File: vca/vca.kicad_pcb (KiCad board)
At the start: 4 copper layers, 95 x 100 mm, 132 parts, among them J2 Conn_ARM_JTAG_SWD_10, U1 LM324, U10 LUM-1502-03_3.5mm_mono_vertic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, U11 LUM-1502-03_3.5mm_mono_vertic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, U12 LUM-1502-03_3.5mm_mono_vertic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, U13 LUM-1502-03_3.5mm_mono_vertic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, U14 LUM-1502-03_3.5mm_mono_vertic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, U15 LUM-1502-03_3.5mm_mono_vertic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, U16 power_conn_16, U17 LUM-1502-03_3.5mm_mono_vertic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, U18 LM7805_TO220, U19 ZLDO1117G33TA, U2 LM324, U20 LUM-1502-03_3.5mm_mono_vertic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, U3 LM324, U4 STM32F103C6Tx, U5 TL074, U6 TL074, U7 TLC7528, U8 LUM-1502-03_3.5mm_mono_vertic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, U9 LUM-1502-03_3.5mm_mono_vertic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, Y1 Crystal_8Mhz

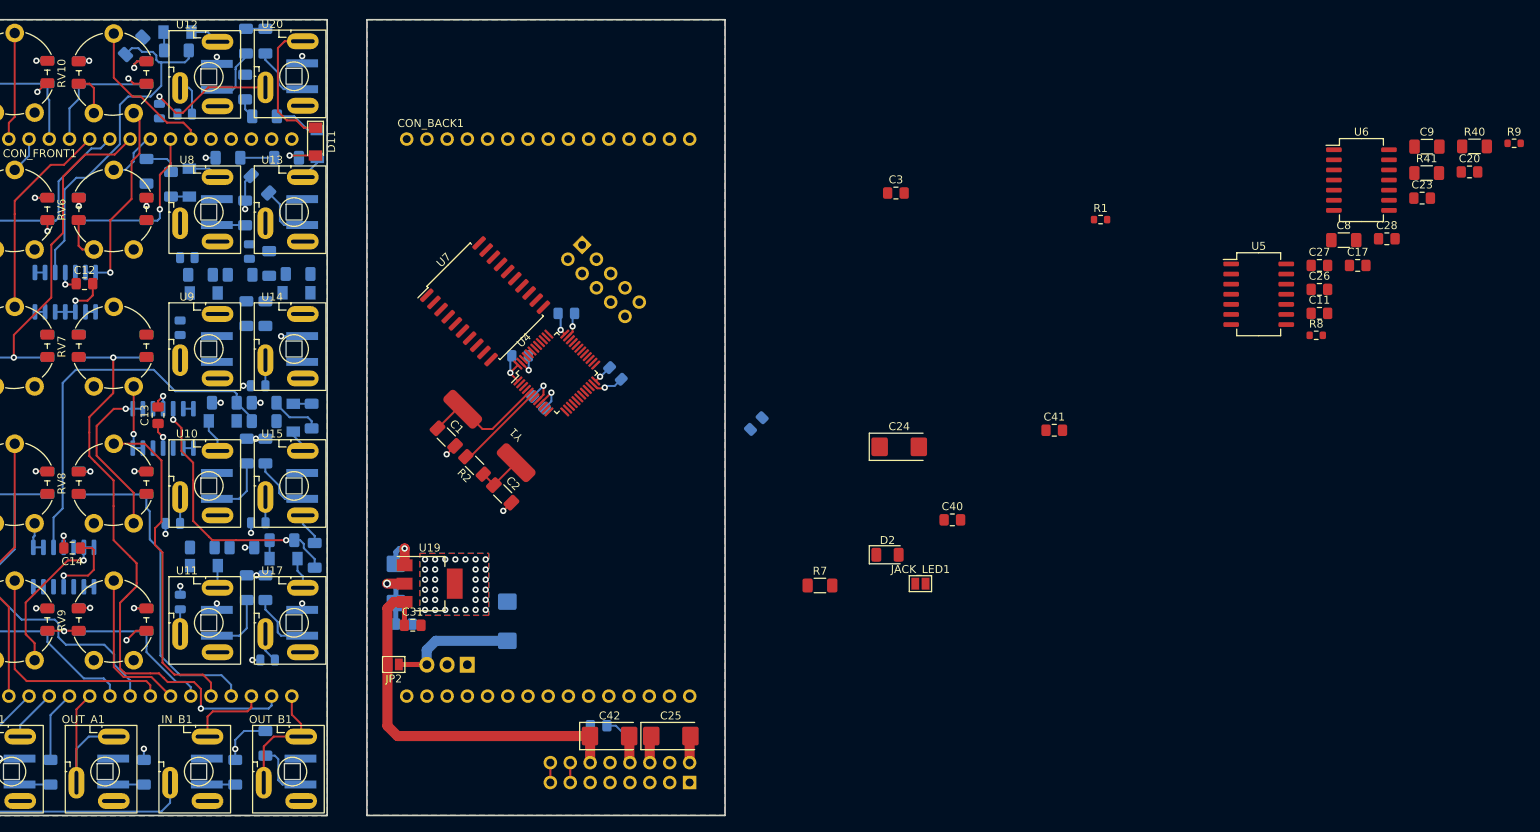
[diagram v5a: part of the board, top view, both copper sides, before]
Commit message: Fixed some pins on the connectors, and working on the back board, power left to go
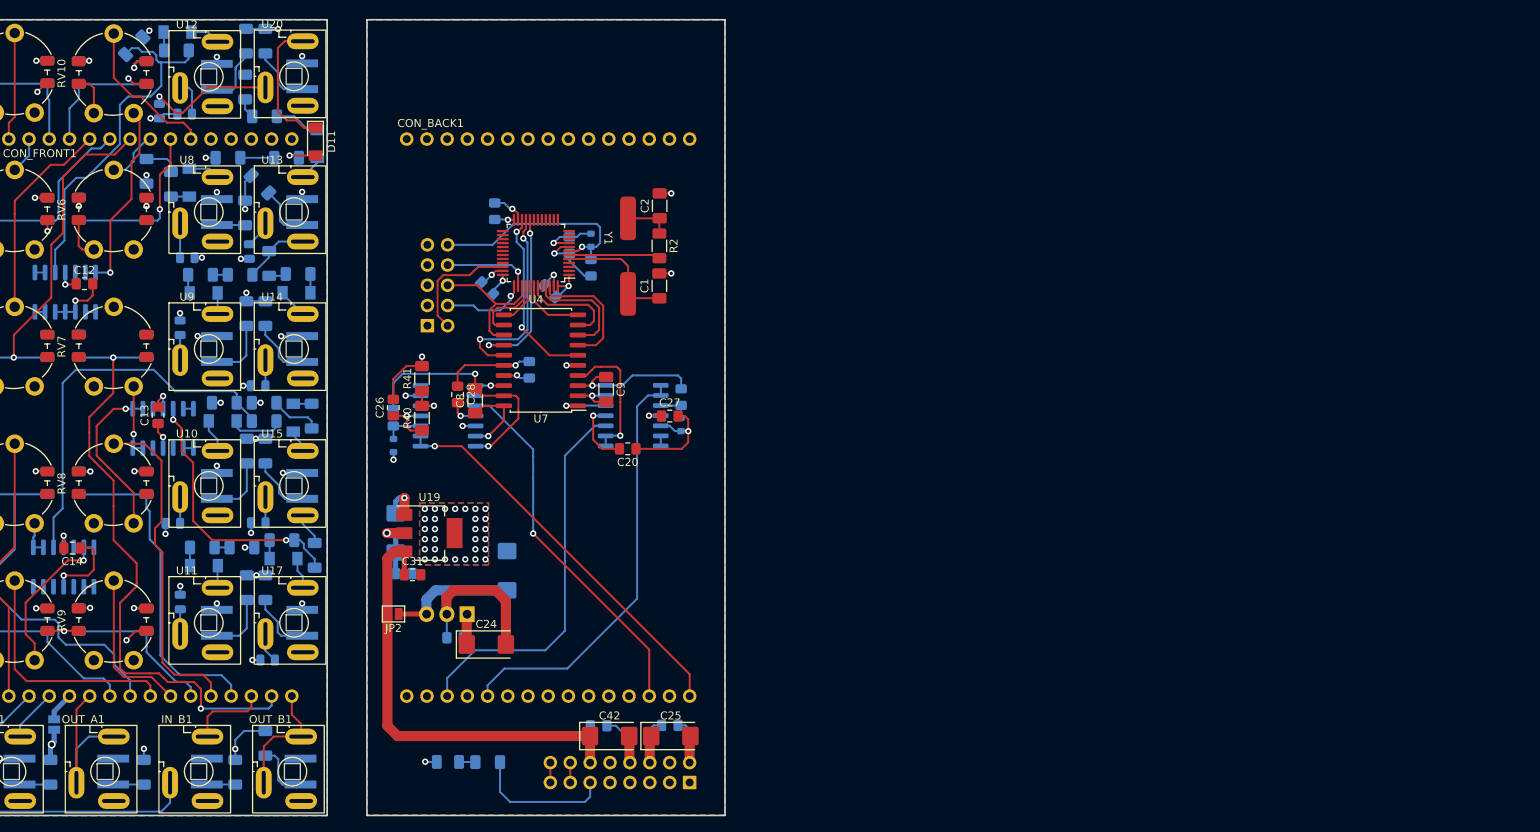
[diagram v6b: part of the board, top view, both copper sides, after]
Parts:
- removed C6: C-100nF-0805, Capacitor_SMD:C_0805_2012Metric_Pad1.18x1.45mm_HandSolder
- C11, C17, C23, C3, C40, C41, D2, JACK_LED1, R1, R7, R8, R9, U5, U6: moved to B.Cu
- moved R9 145.9 mm to (53.3, 53.5), turned to -90 degrees
- moved R40 136.6 mm to (56.9, 50.1), turned to 90 degrees
- moved R41 128.9 mm to (56.9, 45.1), turned to 90 degrees
- moved C17 122.7 mm to (53.3, 50.0), turned to -90 degrees
- moved U6 118.5 mm to (60.2, 49.8)
- moved C28 118.4 mm to (61.4, 47.1), turned to -90 degrees
- moved C26 117.3 mm to (53.3, 48.7), turned to 90 degrees
- moved C20 111.4 mm to (82.8, 53.9), turned to 180 degrees
- moved C8 111.0 mm to (63.6, 47.9), turned to 90 degrees
- moved JACK_LED1 110.3 mm to (10.7, 88.6), turned to -90 degrees
- moved C9 107.6 mm to (80.1, 46.5), turned to -90 degrees
- moved C11 99.5 mm to (70.4, 44.0), turned to 90 degrees
- moved C23 96.4 mm to (89.5, 47.4), turned to -90 degrees
- moved C27 83.8 mm to (88.1, 49.8)
- moved R8 80.6 mm to (89.5, 50.9), turned to -90 degrees
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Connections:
- CON_BACK1 pad 12: unconnected-(CON_BACK1-Pad12) -> +5V
- CON_BACK1 pad 13: unconnected-(CON_BACK1-Pad13) -> GND
- CON_FRONT1 pad 12: unconnected-(CON_FRONT1-Pad12) -> +5C
- CON_FRONT1 pad 13: unconnected-(CON_FRONT1-Pad13) -> GND2
- IN_A1 pad LK: GND -> GND2
- JACK_LED1 pad 1: +12V -> +12VA
- JACK_LED1 pad 2: +12VA -> +12L
- OUT_A1 pad LK: GND -> GND2
- R12 pad 1: +12C -> +12VA
- R15 pad 1: +12C -> +12VA
- R16 pad 1: +12C -> +12VA
- R19 pad 1: +12C -> +12VA
- R22 pad 1: +12C -> +12VA
- R25 pad 1: +12C -> +12VA
- R28 pad 1: +12C -> +12VA
- R3 pad 1: +12VA -> +12L
- R31 pad 1: +12C -> +12VA
- R34 pad 1: +12C -> +12VA
- R37 pad 1: +12C -> +12VA
- R4 pad 1: +12VA -> +12L
- R5 pad 2: +12VA -> +12L
- R6 pad 2: +12VA -> +12L
- U10 pad LK: GND -> GND2
- U11 pad LK: GND -> GND2
- U12 pad LK: GND -> GND2
- U13 pad LK: GND -> GND2
- U14 pad LK: GND -> GND2
- U15 pad LK: GND -> GND2
- U17 pad LK: GND -> GND2
- U20 pad LK: GND -> GND2
- U8 pad LK: GND -> GND2
- U9 pad LK: GND -> GND2
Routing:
- net +12L: track 11.6 -> 192.3 mm, vias 3 -> 8
- net +5C: track 16.1 -> 100.9 mm
- net GND: track 44.6 -> 111.5 mm, vias 13 -> 15
- net B_+10V: track 0.00 -> 59.1 mm, vias 0 -> 1
- net B_OUTA: track 0.00 -> 53.6 mm
- net B_OUTB: track 0.00 -> 49.7 mm, vias 0 -> 1
- net B_INA: track 0.00 -> 48.2 mm
- net B_INB: track 0.00 -> 46.5 mm, vias 0 -> 1
- net Net-(C17-Pad1): track 0.00 -> 31.2 mm, vias 0 -> 2
- net RST: track 0.00 -> 28.3 mm, vias 0 -> 1
- net +5V: track 56.7 -> 84.0 mm, vias 0 -> 1
- net GND2: track 61.9 -> 88.7 mm, vias 12 -> 25
- net CS: track 0.00 -> 25.1 mm, vias 0 -> 2
- net +12V: track 39.2 -> 62.5 mm, vias 0 -> 2
- net DACA/B: track 0.00 -> 22.9 mm, vias 0 -> 2
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
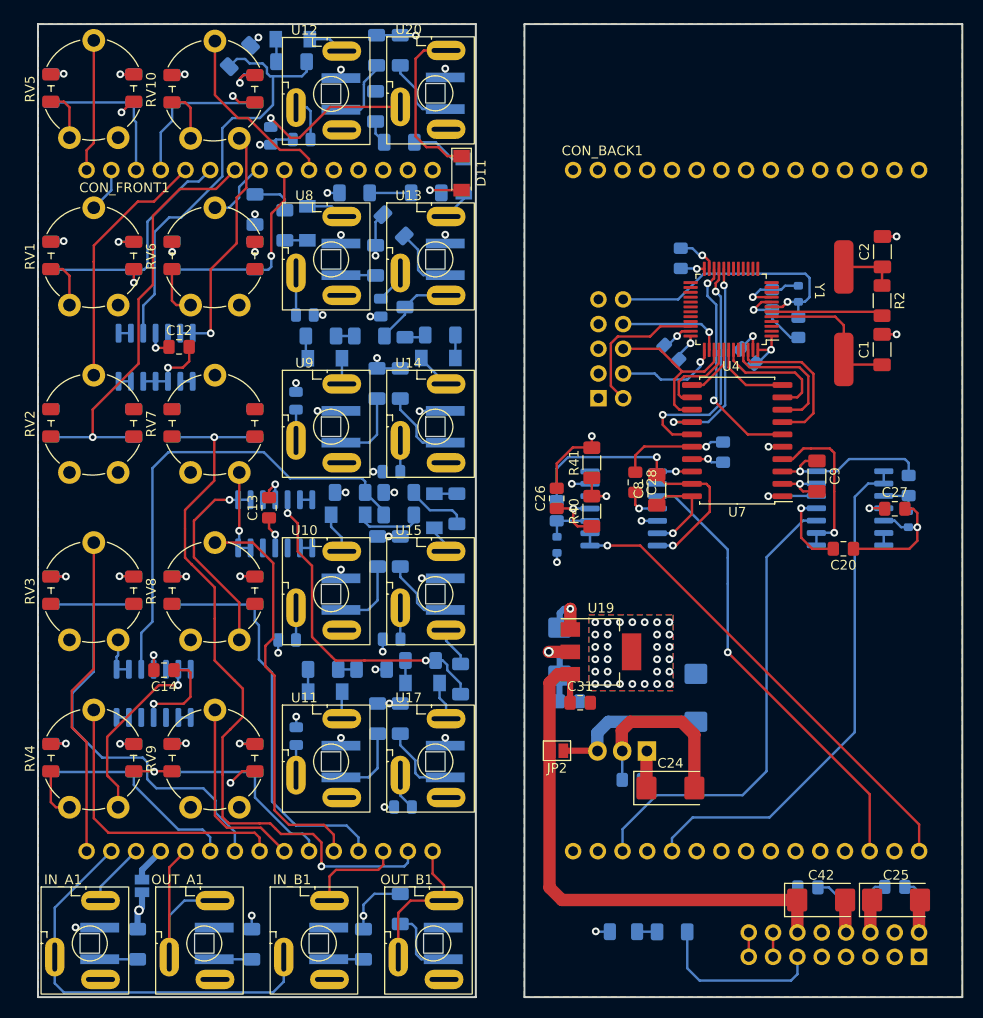
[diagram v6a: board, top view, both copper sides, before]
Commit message: Added buttons, refactored front panel, refactored power part, wip
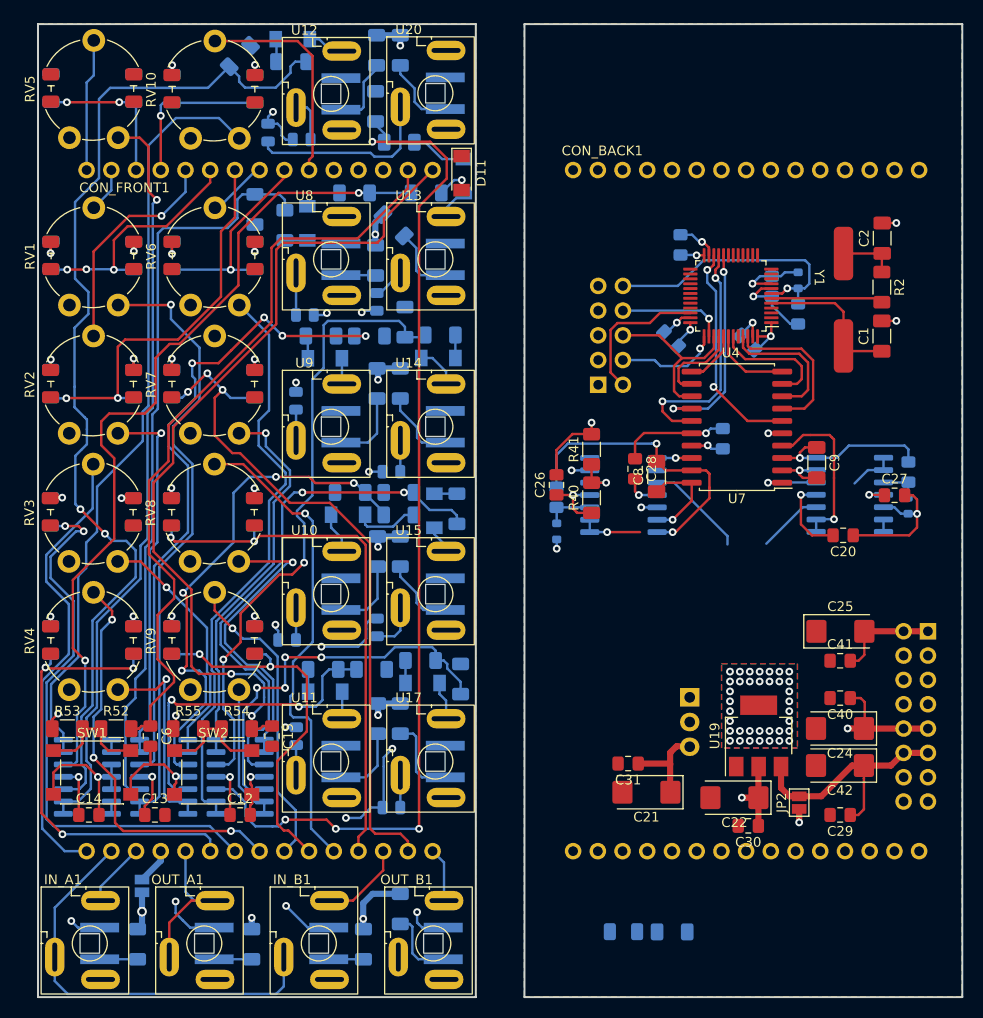
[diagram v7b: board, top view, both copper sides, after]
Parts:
- added C15: C-100nF-0805, Capacitor_SMD:C_0805_2012Metric_Pad1.18x1.45mm_HandSolder, F.Cu at (24.1, 73.2)
- added C6: C-100nF-0805, Capacitor_SMD:C_0805_2012Metric_Pad1.18x1.45mm_HandSolder, F.Cu at (11.6, 73.2)
- added R52: R-100-1206, Resistor_SMD:R_1206_3216Metric_Pad1.30x1.75mm_HandSolder, F.Cu at (8.03, 72.4)
- added R53: R-10k-1206, Resistor_SMD:R_1206_3216Metric_Pad1.30x1.75mm_HandSolder, F.Cu at (3.02, 72.4)
- added R54: R-100-1206, Resistor_SMD:R_1206_3216Metric_Pad1.30x1.75mm_HandSolder, F.Cu at (20.4, 72.4)
- added R55: R-10k-1206, Resistor_SMD:R_1206_3216Metric_Pad1.30x1.75mm_HandSolder, F.Cu at (15.4, 72.4)
- added SW1: SW_Push, Button_Switch_SMD:SW_Push_1P1T_NO_6x6mm_H9.5mm, F.Cu at (5.56, 76.9)
- added SW2: SW_Push, Button_Switch_SMD:SW_Push_1P1T_NO_6x6mm_H9.5mm, F.Cu at (18.0, 76.9)
- C21, C22, C29, C30, C40, C41: moved to F.Cu
- moved C12 48.5 mm to (20.8, 81.3)
- moved U3 43.7 mm to (5.08, 77.4), turned to 0 degrees
- moved C13 33.7 mm to (12.0, 81.3), turned to 0 degrees
- moved U16 33.5 mm to (91.5, 62.4), turned to 180 degrees
- moved C25 28.2 mm to (82.5, 62.4)
- moved U2 26.2 mm to (20.8, 77.4), turned to 0 degrees
- moved JP2 25.5 mm to (78.2, 80.0), turned to 90 degrees
- moved C41 23.9 mm to (82.4, 65.4)
- moved C22 23.4 mm to (71.6, 79.5), turned to 180 degrees
- moved C40 23.0 mm to (82.4, 69.3)
- moved C30 22.4 mm to (73.0, 82.4), turned to 180 degrees
- moved C24 18.5 mm to (82.4, 72.4), turned to 180 degrees
- moved U19 18.4 mm to (74.1, 73.2), turned to 90 degrees
- moved C14 16.8 mm to (5.23, 81.3), turned to 0 degrees
- moved C42 14.0 mm to (82.4, 76.2), turned to 180 degrees
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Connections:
- C31 pad 1: +5V -> Net-(C21-Pad1)
- CON_BACK1 pad 11: unconnected-(CON_BACK1-Pad11) -> +3V3
- CON_BACK1 pad 14: unconnected-(CON_BACK1-Pad14) -> B_BTN_1
- CON_BACK1 pad 15: unconnected-(CON_BACK1-Pad15) -> B_BTN_0
- CON_FRONT1 pad 11: unconnected-(CON_FRONT1-Pad11) -> +3.3VA
- CON_FRONT1 pad 14: unconnected-(CON_FRONT1-Pad14) -> F_BTN_1
- CON_FRONT1 pad 15: unconnected-(CON_FRONT1-Pad15) -> F_BTN_0
- U4 pad 25: unconnected-(U4-Pad25) -> B_BTN_0
- U4 pad 26: unconnected-(U4-Pad26) -> B_BTN_1
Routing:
- net +12VA: track 15.8 -> 174.2 mm, vias 9 -> 10
- net Net-(R26-Pad2): track 2.50 -> 106.1 mm, vias 0 -> 4
- net F_BTN_0: track 0.00 -> 85.7 mm, vias 0 -> 2
- net +3.3VA: track 0.00 -> 85.5 mm, vias 0 -> 2
- net Net-(R38-Pad2): track 4.27 -> 87.1 mm, vias 0 -> 2
- net F_BTN_1: track 0.00 -> 78.4 mm
- net Net-(RV5-Pad1): track 1.27 -> 77.7 mm, vias 0 -> 1
- net Net-(R10-Pad2): track 4.40 -> 76.9 mm
- net Net-(R13-Pad2): track 1.88 -> 69.6 mm, vias 0 -> 4
- net Net-(RV1-Pad1): track 1.27 -> 64.1 mm, vias 0 -> 1
- net Net-(R29-Pad2): track 2.18 -> 64.8 mm, vias 0 -> 2
- net Net-(R23-Pad2): track 44.9 -> 107.4 mm, vias 0 -> 2
- net Net-(RV6-Pad1): track 1.27 -> 60.2 mm
- net B_+10V: track 59.1 -> 3.14 mm
- net +5V: track 84.0 -> 29.0 mm
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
